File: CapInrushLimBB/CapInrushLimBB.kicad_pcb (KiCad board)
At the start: 2 copper layers, 55.7 x 34.9 mm, 31 parts, among them J1 Screw_Terminal_01x02, J2 Screw_Terminal_01x02, K1 G5LE-1A, Q1 MPSA42, Q2 IRF9540N, Q3 TIP41C, Q4 BSP230 300V 0.21A, U1 LM385Z-ADJ

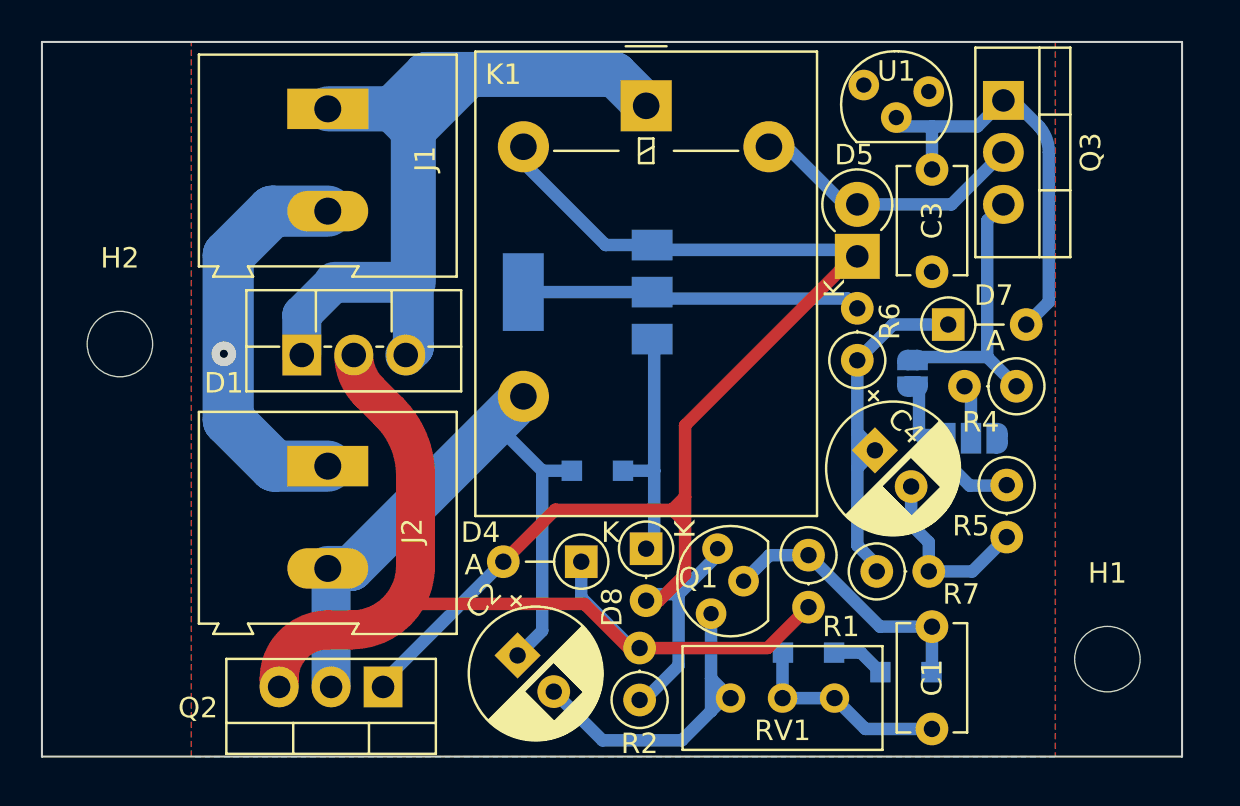
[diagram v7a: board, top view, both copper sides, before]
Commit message: Tweaked track placement.
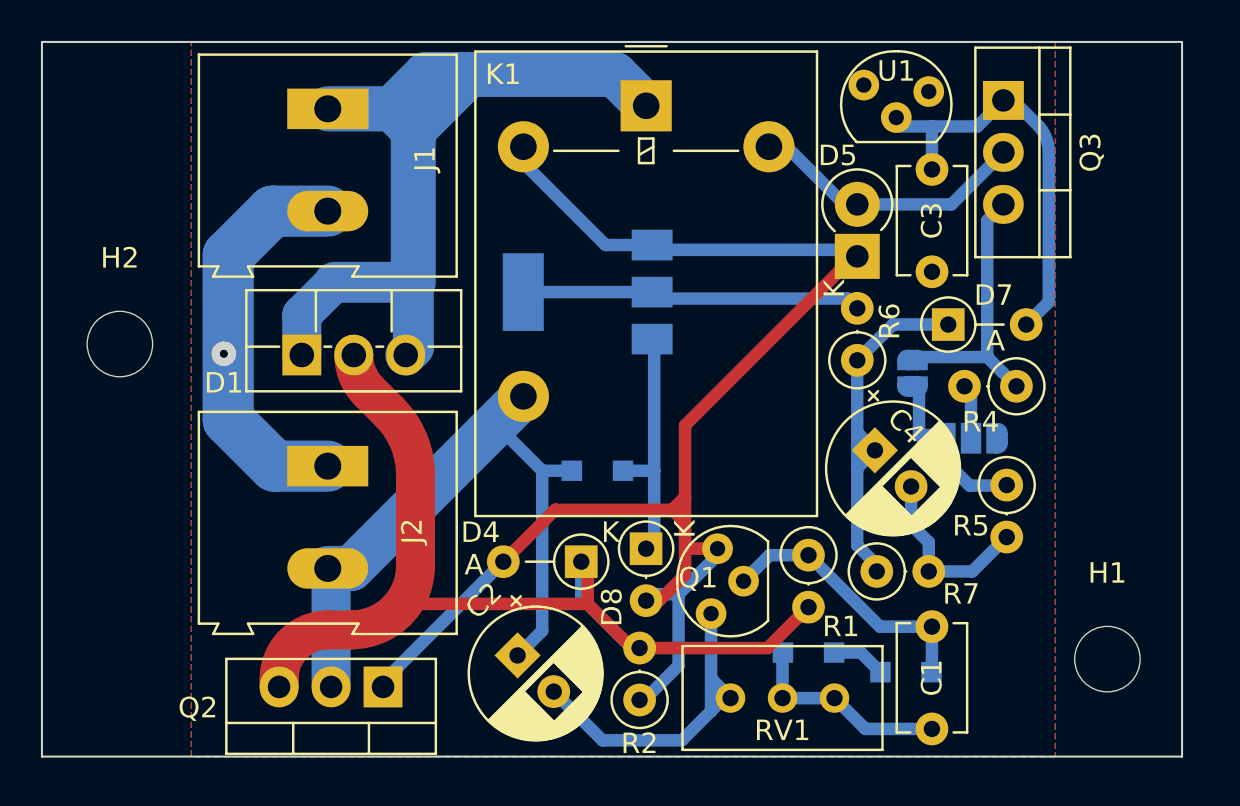
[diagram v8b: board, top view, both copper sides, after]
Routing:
- net /PolProtect: track 48.3 -> 50.3 mm
- net /RLCoilHigh: track 69.8 -> 71.4 mm
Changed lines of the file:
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@@
     (property "Sheetname" "")
     (attr through_hole)
-    (fp_text reference "D5" (at 4.960734 -0.155685 180) (layer "F.SilkS")
+    (fp_text reference "D5" (at 4.92125 -0.9525 180) (layer "F.SilkS")
       (effects (font (size 1 1) (thickness 0.15)))
     )
@@
   (segment (start 225.16 129.725) (end 225.16 137.16) (width 2.2) (layer "B.Cu") (net 5))
   (segment (start 235.008065 127) (end 236.540565 128.5325) (width 2.2) (layer "B.Cu") (net 5))
-  (segment (start 238.4425 151.4475) (end 238.4425 148.904435) (width 0.6096) (layer "F.Cu") (net 6))
-  (segment (start 236.5375 152.7175) (end 237.1725 152.7175) (width 0.6096) (layer "F.Cu") (net 6))
+  (segment (start 238.4425 150.1775) (end 240.03 150.1775) (width 0.6096) (layer "F.Cu") (net 6))
   (segment (start 238.4425 148.904435) (end 238.4425 147.640565) (width 0.6096) (layer "F.Cu") (net 6))
   (segment (start 232.09863 148.2725) (end 229.55863 150.8125) (width 0.6096) (layer "F.Cu") (net 6))
-  (segment (start 237.1725 152.7175) (end 238.4425 151.4475) (width 0.6096) (layer "F.Cu") (net 6))
+  (segment (start 238.4425 148.904435) (end 238.4425 150.1775) (width 0.6096) (layer "F.Cu") (net 6))
   (segment (start 238.4425 148.904435) (end 237.810565 148.2725) (width 0.6096) (layer "F.Cu") (net 6))
   (segment (start 237.810565 148.2725) (end 238.4425 147.640565) (width 0.6096) (layer "F.Cu") (net 6))
   (segment (start 238.4425 147.640565) (end 238.4425 144.148065) (width 0.6096) (layer "F.Cu") (net 6))
+  (segment (start 237.175565 152.7175) (end 238.4425 151.450565) (width 0.6096) (layer "F.Cu") (net 6))
+  (segment (start 238.4425 151.450565) (end 238.4425 150.1775) (width 0.6096) (layer "F.Cu") (net 6))
   (segment (start 238.4425 144.148065) (end 246.700565 135.89) (width 0.6096) (layer "F.Cu") (net 6))
+  (segment (start 236.5375 152.7175) (end 237.175565 152.7175) (width 0.6096) (layer "F.Cu") (net 6))
   (segment (start 237.810565 148.2725) (end 232.09863 148.2725) (width 0.6096) (layer "F.Cu") (net 6))
   (segment (start 236.5375 157.7975) (end 236.22 157.7975) (width 0.6096) (layer "B.Cu") (net 6))
@@
   (segment (start 218.376815 146.1425) (end 216.1125 143.878185) (width 2.5) (layer "B.Cu") (net 11))
   (segment (start 220.98 146.1425) (end 218.376815 146.1425) (width 2.5) (layer "B.Cu") (net 11))
-  (segment (start 236.22 155.0325) (end 235.680565 155.0325) (width 0.6096) (layer "F.Cu") (net 12))
-  (segment (start 233.524315 152.87625) (end 224.793065 152.87625) (width 0.6096) (layer "F.Cu") (net 12))
+  (segment (start 233.683065 152.87625) (end 235.839315 155.0325) (width 0.6096) (layer "F.Cu") (net 12))
+  (segment (start 233.683065 152.87625) (end 233.683065 150.8125) (width 0.6096) (layer "F.Cu") (net 12))
   (segment (start 225.269315 146.576051) (end 225.269315 151.025725) (width 1.905) (layer "F.Cu") (net 12))
   (segment (start 242.4775 155.0325) (end 244.475 153.035) (width 0.6096) (layer "F.Cu") (net 12))
   (segment (start 222.991179 142.501863) (end 223.999315 143.51) (width 1.905) (layer "F.Cu") (net 12))
-  (segment (start 235.680565 155.0325) (end 233.524315 152.87625) (width 0.6096) (layer "F.Cu") (net 12))
   (segment (start 222.14879 154.14625) (end 220.983065 154.14625) (width 1.905) (layer "F.Cu") (net 12))
   (segment (start 242.4775 155.0325) (end 236.22 155.0325) (width 0.6096) (layer "F.Cu") (net 12))
+  (segment (start 224.793065 152.87625) (end 233.683065 152.87625) (width 0.6096) (layer "F.Cu") (net 12))
   (segment (start 218.601815 156.9339) (end 218.601815 156.5275) (width 1.905) (layer "F.Cu") (net 12))
+  (segment (start 235.839315 155.0325) (end 236.22 155.0325) (width 0.6096) (layer "F.Cu") (net 12))
   (arc (start 222.25 140.7125) (mid 222.442626 141.680896) (end 222.991179 142.501863) (width 1.905) (layer "F.Cu") (net 12))
   (arc (start 225.269315 151.025725) (mid 224.355334 153.232269) (end 222.14879 154.14625) (width 1.905) (layer "F.Cu") (net 12))
